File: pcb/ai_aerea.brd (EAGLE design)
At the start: 100 x 100 mm, 26 parts, among them J1 JST-2-MALE, J2 1X02ST, U1 MCP73831

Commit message: routing
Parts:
- added STANDOFF1, STANDOFF2, STANDOFF3, STANDOFF4: STAND-OFF, Ai_Electromechanical:STAND-OFF
- added U$3: AI-LOGOXS, Ai_Miscellany:AI-LOGO-XS
- C1, C2, C3, C4: device Ai_Passives:CAP-0603 -> Ai_Passives:CAP-025X050
- D1: device Ai_DiscreteSemis:SMA-403D -> Ai_DiscreteSemis:TH-1N914
- LED1, LED2, LED3, LED4, LED5, LED6: device Ai_LED:LED-0805 -> Ai_LED:LED-5MM
- R1, R3, R4, R5, R6, R7: device Ai_Passives:RES-0603 -> Ai_Passives:RES-AXIAL-0.4
- moved R7 182.3 mm to (33.5, 91.6), flipped to the bottom, turned to 335 degrees
- moved C4 168.1 mm to (93.7, 64.0), flipped to the bottom, turned to 250 degrees
- moved Q2 164.3 mm to (73.3, 87.8), flipped to the bottom, turned to 300 degrees
- moved R4 155.4 mm to (93.8, 39.4), flipped to the bottom, turned to 280 degrees
- moved R3 150.7 mm to (62.0, 93.0), flipped to the bottom, turned to 15 degrees
- moved R5 146.4 mm to (10.0, 65.2), flipped to the bottom, turned to 290 degrees
- moved C3 144.9 mm to (42.5, 94.8), flipped to the bottom, turned to 350 degrees
- moved Q1 143.3 mm to (95.0, 50.0), flipped to the bottom
- moved R6 141.2 mm to (73.5, 10.6), flipped to the bottom, turned to 330 degrees
- moved LED2 139.8 mm to (89.0, 73.0), turned to 210 degrees
- moved LED1 131.8 mm to (50.0, 95.0), turned to 270 degrees
- moved LED6 131.0 mm to (11.0, 73.0), turned to 330 degrees
- moved LED3 116.7 mm to (89.0, 27.0), turned to 150 degrees
- moved VR1 112.0 mm to (23.5, 87.0), turned to 220 degrees
- moved Q3 105.0 mm to (61.3, 5.30), flipped to the bottom, turned to 90 degrees
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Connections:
- net +: now also R3.P$2, R4.P$2; no longer R3.2, R4.2
- net -: now also R7.P$1; no longer R7.1
- net GND: now also R1.P$1; no longer R1.1
- net N$10: now also R5.P$1, R7.P$2; no longer R5.1, R7.2
- net N$12: now also R6.P$2; no longer R6.2
- net N$13: now also R6.P$1; no longer R6.1
- net N$3: now also R1.P$2; no longer R1.2
- net N$6: now also R3.P$1; no longer R3.1
- net N$7: now also R4.P$1; no longer R4.1
- net VBAT: now also R5.P$2; no longer R5.2
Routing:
- net +: track 0.00 -> 342.4 mm
- net N$9: track 0.00 -> 195.6 mm, vias 0 -> 2
- net -: track 0.00 -> 105.1 mm
- net VBAT: track 0.00 -> 102.6 mm, vias 0 -> 1
- net N$14: track 0.00 -> 98.2 mm
- net N$13: track 0.00 -> 64.6 mm
- net N$10: track 0.00 -> 56.8 mm
- net N$6: track 0.00 -> 41.3 mm
- net N$7: track 0.00 -> 21.3 mm
- net N$2: track 0.00 -> 14.3 mm
- net N$3: track 0.00 -> 9.16 mm
- net N$1: track 0.00 -> 8.44 mm
- net N$12: track 0.00 -> 5.90 mm
- added copper zone on layer 1, net GND
- added copper zone on layer 16, net GND

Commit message: routed
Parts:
- moved VR1 1.37 mm to (24.4, 85.9), flipped to the bottom, turned to 322.5 degrees
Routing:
- net N$10: track 56.8 -> 127.7 mm, vias 0 -> 1
- net N$9: track 195.6 -> 199.1 mm
- net VBAT: track 102.6 -> 103.6 mm, vias 1 -> 2
- net -: track 105.1 -> 106.1 mm
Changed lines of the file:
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@@
 <layer number="23" name="tOrigins" color="15" fill="1" visible="yes" active="yes"/>
 <layer number="24" name="bOrigins" color="15" fill="1" visible="yes" active="yes"/>
-<layer number="25" name="tNames" color="7" fill="1" visible="no" active="yes"/>
-<layer number="26" name="bNames" color="7" fill="1" visible="no" active="yes"/>
+<layer number="25" name="tNames" color="7" fill="1" visible="yes" active="yes"/>
+<layer number="26" name="bNames" color="7" fill="1" visible="yes" active="yes"/>
 <layer number="27" name="tValues" color="7" fill="1" visible="no" active="yes"/>
 <layer number="28" name="bValues" color="7" fill="1" visible="no" active="yes"/>
@@
 <element name="R1" library="Ai_Passives" package="RES-AXIAL-0.4" value="2K" x="6.74" y="66.26" rot="MR290"/>
 <element name="R2" library="Ai_Sensors" package="LDR" value="LDR-PTH" x="34.01" y="8.01" rot="R157.5"/>
-<element name="VR1" library="Ai_Passives" package="POT-05X05" value="" x="23.51" y="86.99" rot="R220"/>
+<element name="VR1" library="Ai_Passives" package="POT-05X05" value="" x="24.39" y="85.94" rot="MR322.5"/>
 <element name="LED1" library="Ai_LED" package="LED-5MM" value="" x="50" y="95" locked="yes" rot="R270"/>
 <element name="LED2" library="Ai_LED" package="LED-5MM" value="" x="89" y="73" locked="yes" rot="R210"/>
@@
 <contactref element="J2" pad="2"/>
 <contactref element="D1" pad="A"/>
-<wire x1="9.420971875" y1="38.914671875" x2="9.45" y2="34.35" width="0.254" layer="1"/>
-<wire x1="9.45" y1="34.35" x2="8.769696875" y2="30.533209375" width="0.254" layer="1"/>
+<wire x1="9.420971875" y1="38.914671875" x2="9.4" y2="32.35" width="0.254" layer="1"/>
+<wire x1="9.4" y1="32.35" x2="8.769696875" y2="30.533209375" width="0.254" layer="1"/>
 </signal>
 <signal name="N$2">
@@
 <wire x1="5.25" y1="46.15" x2="5.229834375" y2="55.0106875" width="0.254" layer="1"/>
 </signal>
-<signal name="GND" airwireshidden="yes">
+<signal name="GND">
 <contactref element="C1" pad="2"/>
 <contactref element="J1" pad="2"/>
@@
 <vertex x="100" y="0"/>
 </polygon>
-<wire x1="2.5" y1="47.6" x2="7.76016875" y2="54.789309375" width="0" layer="19" extent="16-16"/>
 </signal>
 <signal name="N$3">
@@
 <wire x1="7.6" y1="25.5" x2="1.7" y2="41.45" width="0.254" layer="16"/>
 <wire x1="1.7" y1="41.45" x2="1.7" y2="45.1" width="0.254" layer="16"/>
-<wire x1="1.7" y1="45.1" x2="2.35" y2="46.35" width="0.254" layer="16"/>
+<wire x1="1.7" y1="45.1" x2="2.25" y2="45.8" width="0.254" layer="16"/>
 <wire x1="2.5" y1="49.6" x2="3.05" y2="49.6" width="0.254" layer="16"/>
-<wire x1="3.05" y1="49.6" x2="5.65" y2="49.6" width="0.254" layer="16"/>
-<wire x1="5.65" y1="49.6" x2="6.2" y2="48.65" width="0.254" layer="16"/>
-<wire x1="6.2" y1="48.65" x2="6.2" y2="47.4" width="0.254" layer="16"/>
-<wire x1="6.2" y1="47.4" x2="5.75" y2="46.35" width="0.254" layer="16"/>
-<wire x1="5.75" y1="46.35" x2="2.35" y2="46.35" width="0.254" layer="16"/>
-<wire x1="21.564246875" y1="85.35731875" x2="19.8" y2="87.55" width="0.254" layer="16"/>
-<wire x1="19.8" y1="87.55" x2="18.5" y2="87.5" width="0.254" layer="16"/>
+<wire x1="3.05" y1="49.6" x2="5.25" y2="49.6" width="0.254" layer="16"/>
+<wire x1="5.25" y1="49.6" x2="6.2" y2="48.55" width="0.254" layer="16"/>
+<wire x1="6.2" y1="48.55" x2="6.2" y2="46.75" width="0.254" layer="16"/>
+<wire x1="6.2" y1="46.75" x2="5.2" y2="45.8" width="0.254" layer="16"/>
+<wire x1="5.2" y1="45.8" x2="2.25" y2="45.8" width="0.254" layer="16"/>
+<wire x1="22.374884375" y1="84.39374375" x2="20.4" y2="87.25" width="0.254" layer="1"/>
+<wire x1="20.4" y1="87.25" x2="18.5" y2="87.5" width="0.254" layer="16"/>
 <wire x1="18.5" y1="87.5" x2="7.6" y2="74.5" width="0.254" layer="16"/>
 <wire x1="7.6" y1="74.5" x2="4.8" y2="66.9" width="0.254" layer="16"/>
@@
 <wire x1="3.05" y1="50.95" x2="3.05" y2="49.6" width="0.254" layer="16"/>
 <wire x1="8.262540625" y1="60.386359375" x2="5.694296875" y2="58.31553125" width="0.254" layer="16"/>
+<via x="20.4" y="87.25" extent="1-16" drill="0.508"/>
 </signal>
 <signal name="N$6">
@@
 <wire x1="79.45" y1="87.3" x2="74.1" y2="90.45" width="0.254" layer="1"/>
 <wire x1="74.1" y1="90.45" x2="71.080296875" y2="89.12" width="0.254" layer="1"/>
-<wire x1="12.09985" y1="27.635" x2="6.45" y2="41.35" width="0.254" layer="16"/>
 <via x="6.45" y="41.35" extent="1-16" drill="0.508"/>
 <wire x1="6.45" y1="41.35" x2="6.45" y2="54.8" width="0.254" layer="1"/>
@@
 <wire x1="21.85" y1="19.6" x2="32.1" y2="11.55" width="0.254" layer="1"/>
 <wire x1="32.1" y1="11.55" x2="50" y2="6.27" width="0.254" layer="1"/>
+<wire x1="12.09985" y1="27.635" x2="7.4" y2="28.8" width="0.254" layer="16"/>
+<wire x1="7.4" y1="28.8" x2="4.45" y2="36.35" width="0.254" layer="16"/>
+<wire x1="4.45" y1="36.35" x2="6.45" y2="41.35" width="0.254" layer="16"/>
 </signal>
 <signal name="N$10">
@@
 <contactref element="Q3" pad="2"/>
 <contactref element="R7" pad="P$2"/>
-<wire x1="32.162240625" y1="8.775365625" x2="11.7374625" y2="69.9336375" width="0" layer="19" extent="1-1"/>
 <wire x1="28.905959375" y1="89.443096875" x2="27.4" y2="84.75" width="0.254" layer="1"/>
 <wire x1="27.4" y1="84.75" x2="19.3" y2="78.95" width="0.254" layer="1"/>
@@
 <wire x1="32.55" y1="8.55" x2="56.35" y2="8.55" width="0.254" layer="16"/>
 <wire x1="56.35" y1="8.55" x2="61.32" y2="5.3" width="0.254" layer="16"/>
+<wire x1="11.7374625" y1="69.9336375" x2="9.9" y2="61.35" width="0.254" layer="1"/>
+<wire x1="9.9" y1="61.35" x2="7.65" y2="44.3" width="0.254" layer="1"/>
+<wire x1="7.65" y1="44.3" x2="7.65" y2="36.25" width="0.254" layer="1"/>
+<via x="7.65" y="36.25" extent="1-16" drill="0.508"/>
+<wire x1="7.65" y1="36.25" x2="14.35" y2="27.7" width="0.254" layer="16"/>
+<wire x1="14.35" y1="27.7" x2="32.162240625" y2="8.775365625" width="0.254" layer="16"/>
 </signal>
 <signal name="N$12">
@@
 <contactref element="Q1" pad="1"/>
 <contactref element="Q2" pad="1"/>
-<wire x1="25.142678125" y1="85.044246875" x2="38.11404375" y2="93.7369" width="0.254" layer="16"/>
+<wire x1="22.843746875" y1="87.955115625" x2="29.6" y2="92.1" width="0.254" layer="1"/>
+<wire x1="29.6" y1="92.1" x2="38.11404375" y2="93.7369" width="0.254" layer="1"/>
 <wire x1="38.11404375" y1="93.7369" x2="40.7" y2="97.35" width="0.254" layer="16"/>
 <wire x1="40.7" y1="97.35" x2="50" y2="99" width="0.254" layer="16"/>

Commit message: gerbers generated
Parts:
- removed VR1: (no value), Ai_Passives:POT-05X05
- added BRT: (no value), Ai_Passives:POT-05X05
- added U$4: AI-LOGOM, Ai_Miscellany:AI-LOGO-M
- U$3: value AI-LOGOXS -> AI-LOGOM; device Ai_Miscellany:AI-LOGO-XS -> Ai_Miscellany:AI-LOGO-M
- moved U$3 13.0 mm to (74.4, 14.0), turned to 210 degrees
- moved R4 1.85 mm to (93.2, 37.7)
- moved J2 0.68 mm to (7.90, 32.8)
- moved R1 0.62 mm to (6.14, 66.4)
- moved R5 0.52 mm to (9.50, 65.3)
- turned Q3 to 75 degrees
- renumbered R2 to LDR
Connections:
- net N$1 renamed VPANEL
- net -: now also BRT.2; no longer VR1.2
- net GND: now also BRT.1; no longer VR1.1
- net VBAT: now also BRT.3; no longer VR1.3
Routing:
- net N$7: track 21.3 -> 24.0 mm
- net +: track 342.4 -> 340.7 mm
- net VBAT: track 103.6 -> 102.4 mm
- net N$3: track 9.16 -> 8.62 mm
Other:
- board text added: "+"
- board text added: "-"
- board text added: "Pasadena, CA"
- board text added: "v1.0"
- board text added: "www.acrobotic.com"

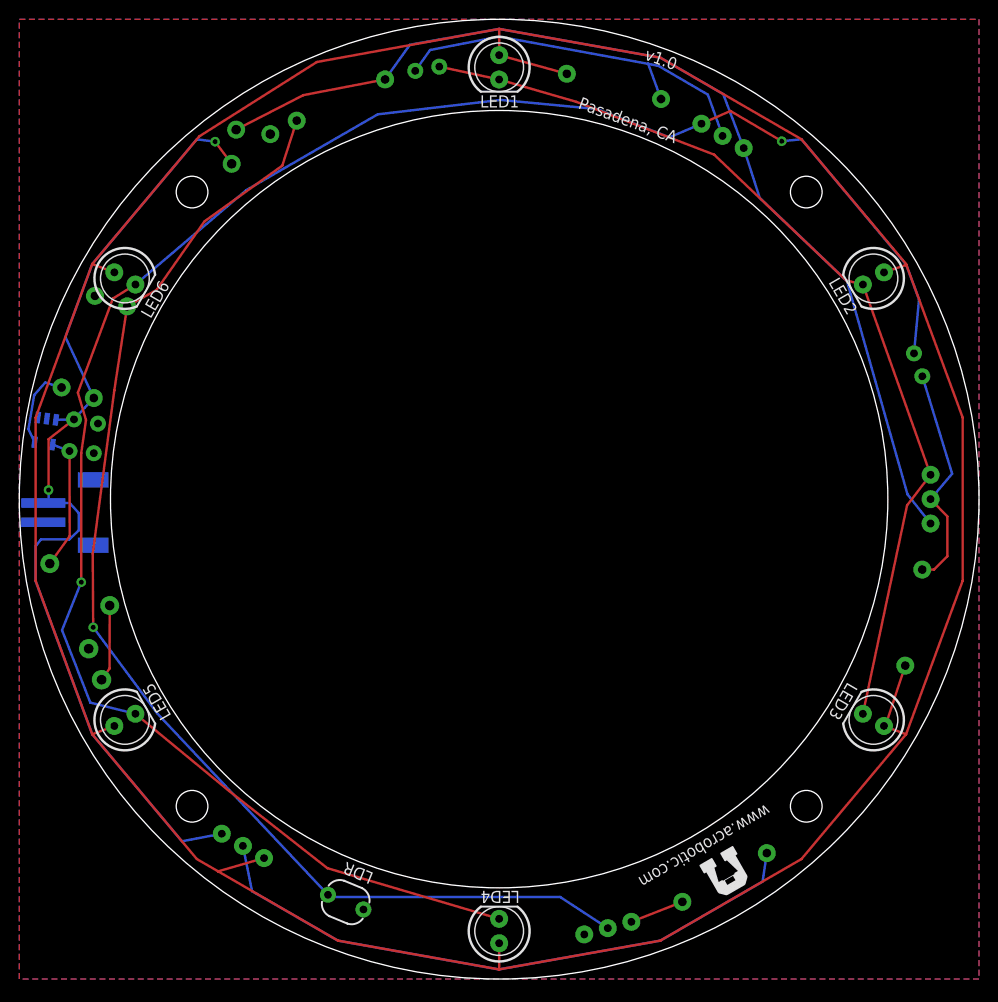
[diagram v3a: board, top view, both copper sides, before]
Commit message: going with a square design
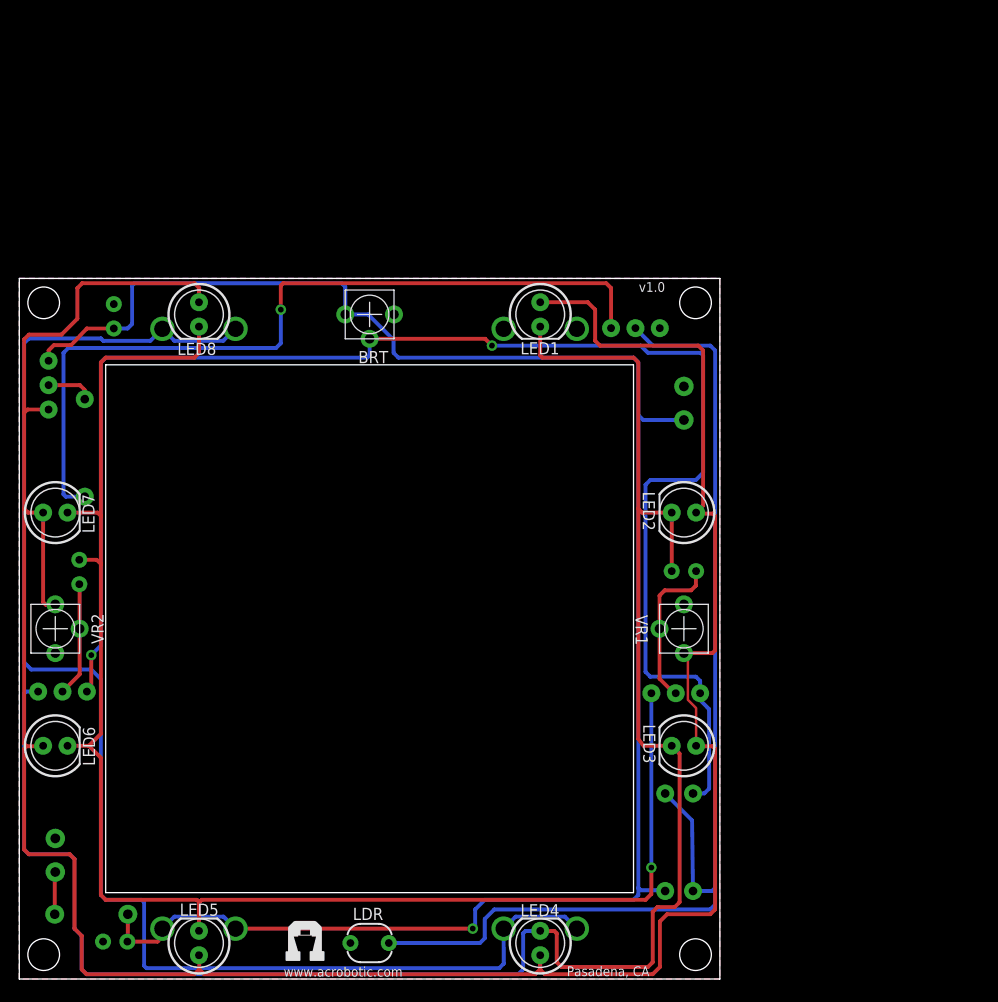
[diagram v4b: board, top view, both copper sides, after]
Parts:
- removed J1: JST-2-MALE, Ai_Connectors:JST-2-SMD
- removed J2: 1X02ST, Ai_Connectors:1X02-ST
- removed R1: 2K, Ai_Passives:RES-AXIAL-0.4
- removed R3, R4: 47K, Ai_Passives:RES-AXIAL-0.4
- removed U1: MCP73831, Ai_IC:SOT23-5
- added BAT1, BAT2: (no value), Ai_Electromechanical:BATTERY-AAA
- added BATT, PANEL: 1X02ST, Ai_Connectors:1X02-ST
- added LED7, LED8: (no value), Ai_LED:LED-5MM
- added VR1, VR2: (no value), Ai_Passives:POT-05X05
- moved Q1 92.6 mm to (4.50, 29.9), turned to 270 degrees
- moved C4 90.0 mm to (6.25, 42.4), turned to 270 degrees
- moved R7 85.6 mm to (70.2, 14.2), turned to 270 degrees
- moved STANDOFF3 81.0 mm to (2.54, 2.54)
- moved R6 80.3 mm to (6.82, 55.3), turned to 270 degrees
- moved R5 77.1 mm to (67.3, 14.2), turned to 270 degrees
- moved Q3 62.6 mm to (64.2, 67.8), turned to 270 degrees
- moved C3 58.8 mm to (69.2, 42.5), turned to 180 degrees
- moved Q2 58.3 mm to (68.4, 29.8), turned to 270 degrees
- moved STANDOFF1 54.7 mm to (2.54, 70.5)
- moved Q4 52.1 mm to (3.05, 61.9), turned to 180 degrees
- moved C1 51.1 mm to (9.99, 3.90), turned to 0 degrees
- moved LED6 49.2 mm to (3.75, 24.3), turned to 0 degrees
- moved U$3 48.3 mm to (27.6, 1.78), turned to 0 degrees
- moved D1 34.4 mm to (7.50, 6.75), turned to 180 degrees
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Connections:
- removed net N$2: C1.1, D1.C, U1.4
- removed net N$9: C4.1, LED4.C, LED5.C, LED6.C, Q2.3
- removed net VSS: U1.2
- new net N$1: BAT1.GND@1, BAT1.GND@2, BAT2.PWR@1, BAT2.PWR@2
- net +: now also LED7.A, LED8.A, VR1.1, VR2.1; no longer R3.P$2, R4.P$2
- net GND: now also BAT2.GND@1, BAT2.GND@2, BATT.2, PANEL.1; no longer J1.2, J2.1, R1.P$1
- net N$14: now also LED4.C
- net N$3: now also C4.1, LED5.C, LED6.C, LED7.C, LED8.C, Q2.3; no longer R1.P$2, U1.5
- net N$6: now also VR1.2; no longer R3.P$1
- net N$7: now also VR2.2; no longer R4.P$1
- net VBAT: now also BAT1.PWR@1, BAT1.PWR@2, BATT.1, C1.1, D1.C; no longer J1.1, U1.3
- net VPANEL: now also PANEL.2; no longer J2.2
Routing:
- net N$9: track 199.6 -> 0.00 mm, vias 2 -> 0
- net N$3: track 8.62 -> 160.1 mm, vias 0 -> 1
- net N$1: track 0.00 -> 149.9 mm
- net N$14: track 98.2 -> 194.0 mm
- net VBAT: track 102.4 -> 198.0 mm, vias 2 -> 1
- net N$12: track 5.71 -> 85.0 mm, vias 0 -> 1
- net +: track 340.7 -> 276.1 mm
- net N$13: track 64.6 -> 4.94 mm
- net -: track 106.1 -> 158.2 mm, vias 0 -> 2
- net N$6: track 41.3 -> 16.7 mm
- net N$2: track 14.3 -> 0.00 mm
- net N$7: track 24.0 -> 11.9 mm
- net N$10: track 128.1 -> 117.6 mm, vias 1 -> 0
- net VPANEL: track 8.00 -> 4.42 mm
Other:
- board size 100 x 100 mm -> 73 x 73 mm
